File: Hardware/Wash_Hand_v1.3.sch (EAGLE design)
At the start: 32 parts, among them J1 I2C, J2 ICSP, J3 SPI, J5 EXT_VCC, J6 6_PIN_SERIAL_CABLEPTH, Q1 16.0 Mhz, U1 328P

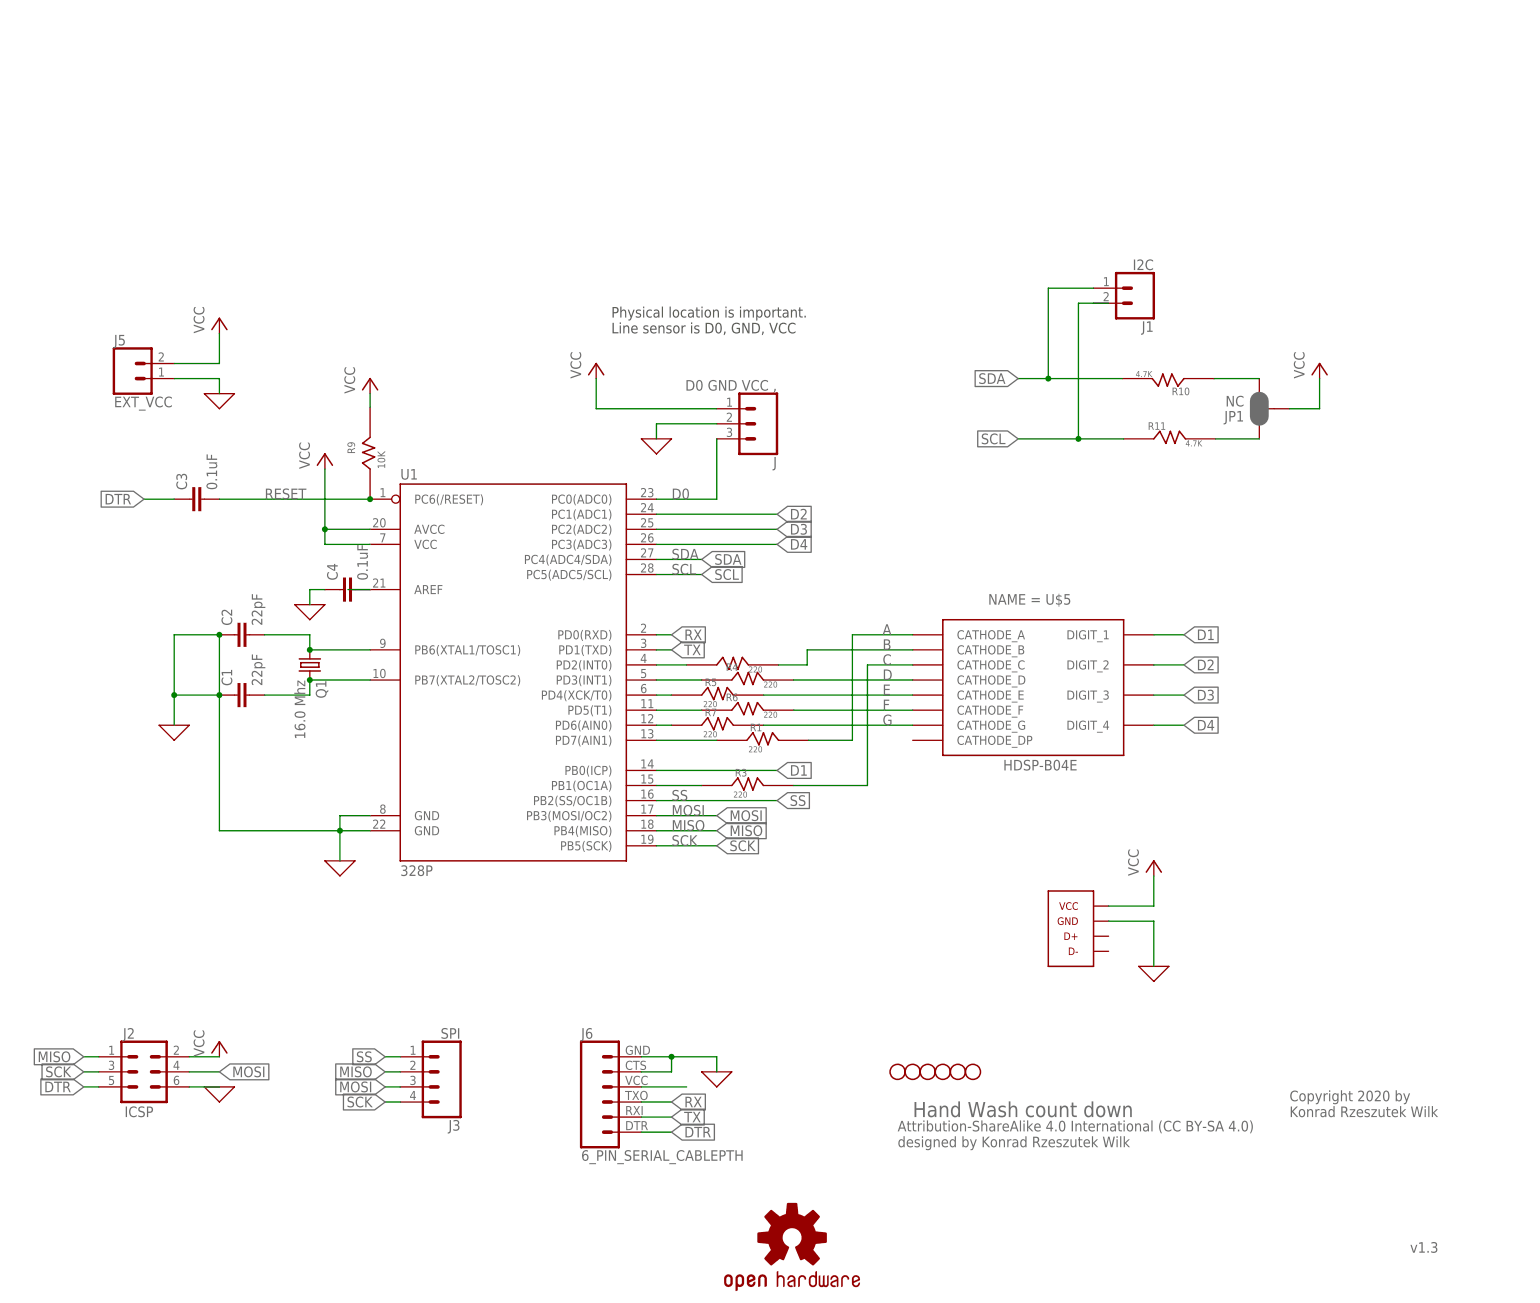
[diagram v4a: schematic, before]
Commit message: Board/Schematic: Add MIC5205 linear voltage regulator
Which also meant we had to:
 - Move resistors and capacitors around.
 - Move on the schematic the components around.
 - Instead of a switch I just added a solder pad to isolate the USB when not needed.

Signed-off-by: Konrad Rzeszutek Wilk <konrad@kernel.org>
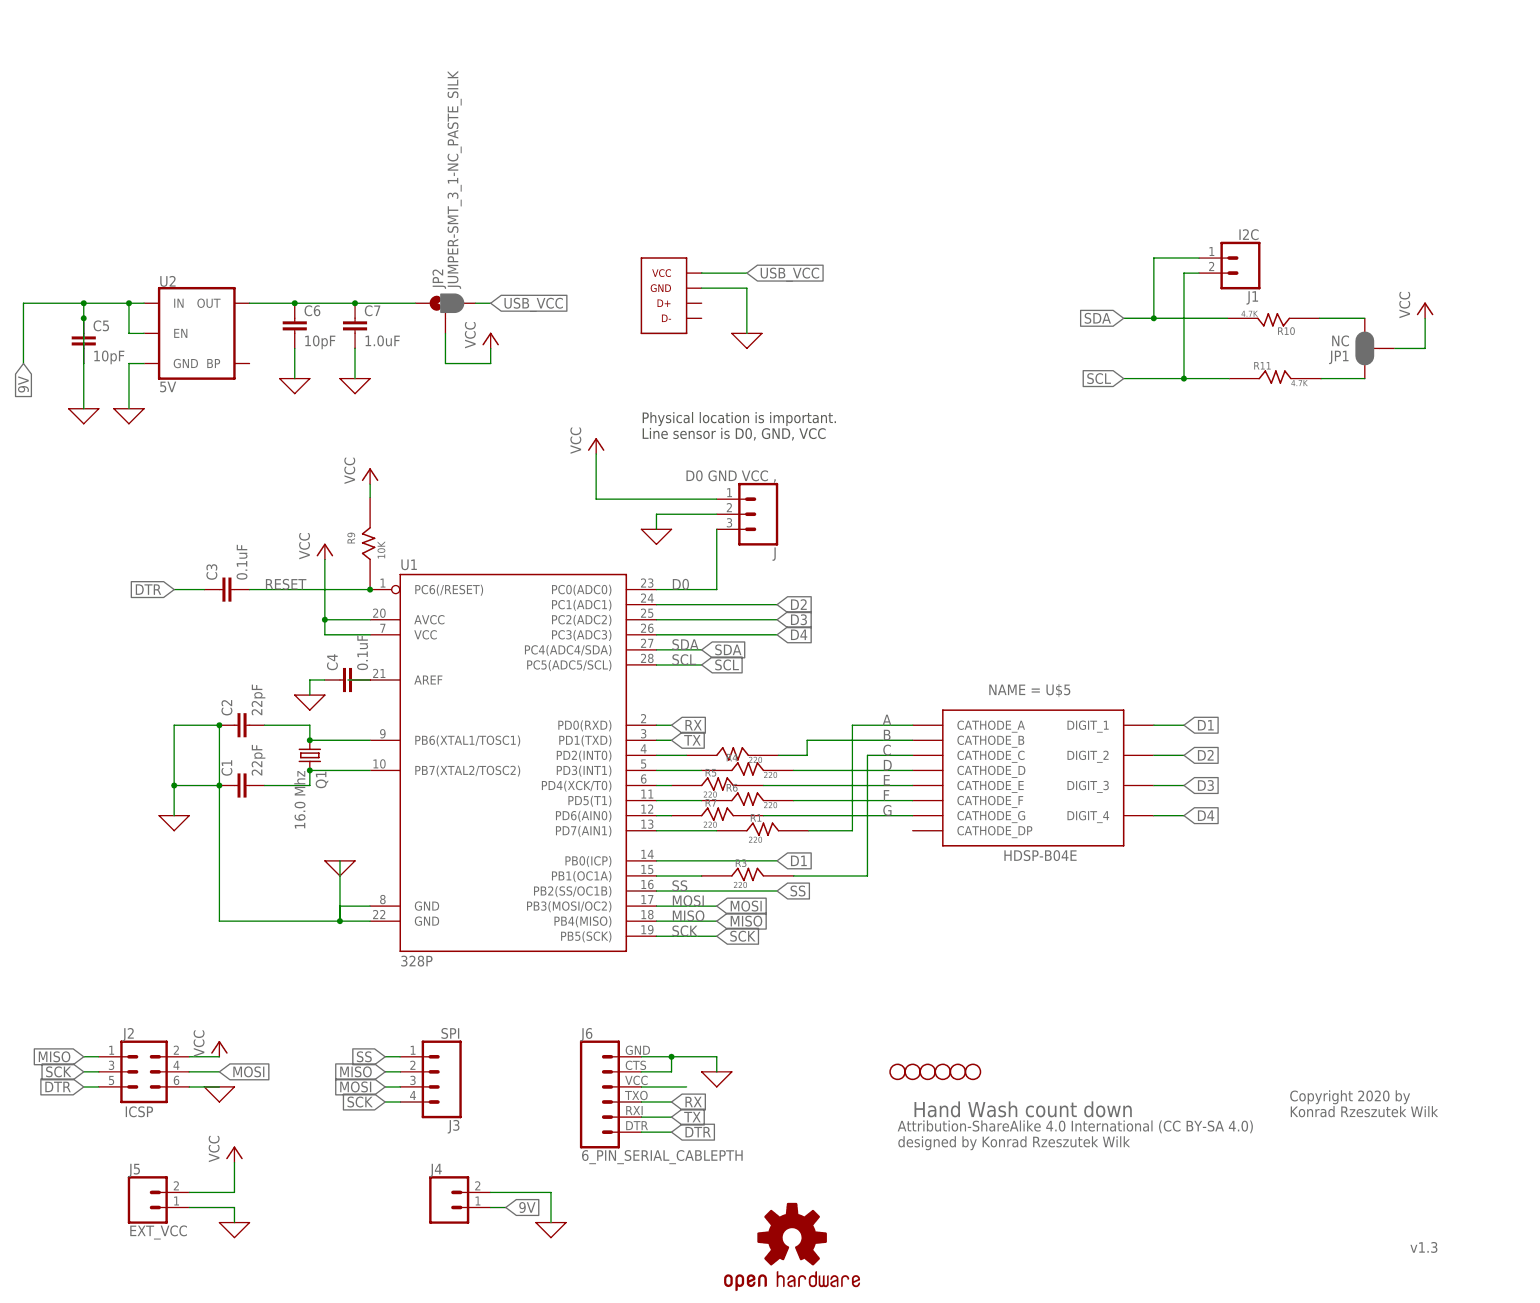
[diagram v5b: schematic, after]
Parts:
- added C5, C6: 10pF, SparkFun-Capacitors:1.0UF-1206-50V-10%
- added C7: 1.0uF, SparkFun-Capacitors:1.0UF-1206-50V-10%
- added J4: (no value), SparkFun-Connectors:CONN_02
- added JP2: JUMPER-SMT_3_1-NC_PASTE_SILK, SparkFun-Jumpers:JUMPER-SMT_3_1-NC_PASTE_SILK
- added U2: 5V, SparkFun-IC-Power:V_REG_MIC52055V
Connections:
- new net 9V: C5.1, C5.2, J4.1, U2.EN, U2.IN
- new net N$10: C6.1, C7.1, JP2.1, U2.OUT
- new net USB_VCC: JP2.3, U$4.VCC
- net 0: now also C6.2, C7.2, J4.2, U2.GND
- net VCC: now also JP2.2; no longer U$4.VCC
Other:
- moved on the sheet: C1, C2, C3, C4, J, J1, J5, JP1, NAME = U$5, Q1, R1, R10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

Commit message: Board/Schematic: Add line sensor.
We are using QRE1113GR.

Signed-off-by: Konrad Rzeszutek Wilk <konrad@kernel.org>
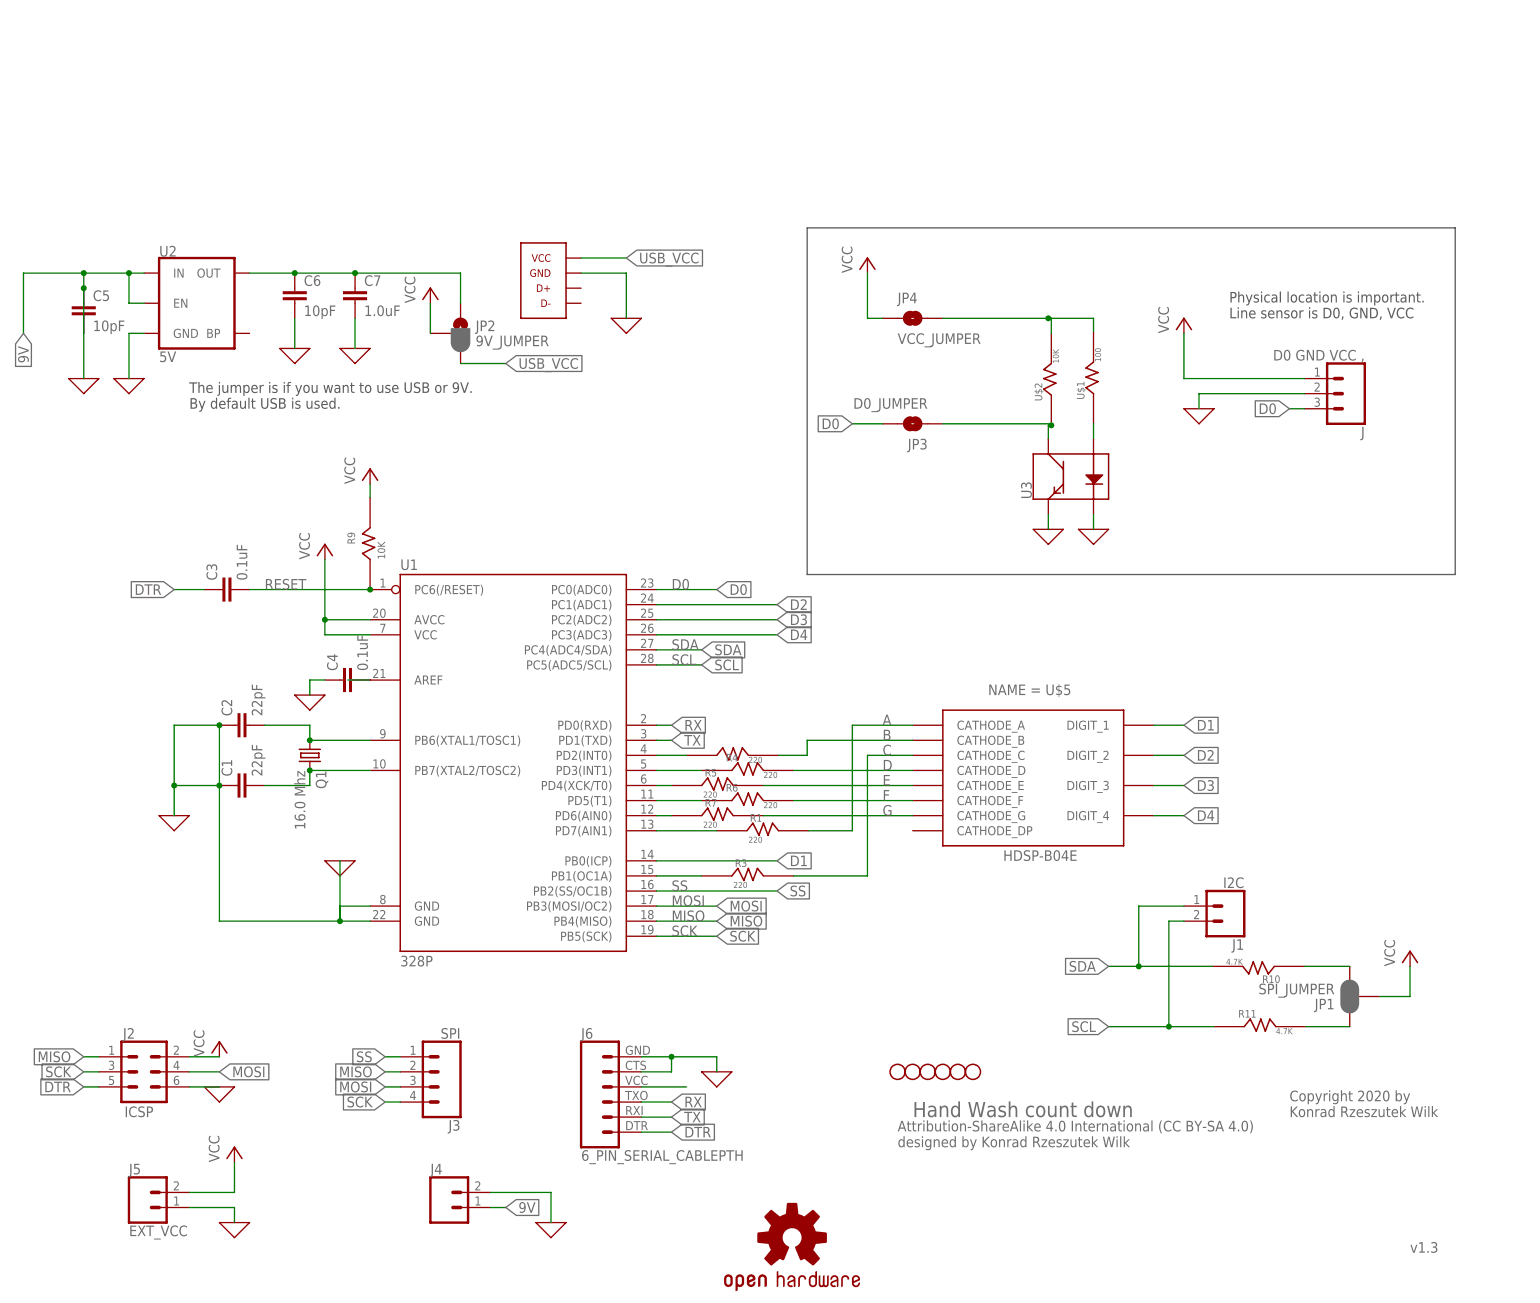
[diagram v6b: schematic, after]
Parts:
- added JP3: D0_JUMPER, SparkFun-Jumpers:JUMPER-SMT_2_NO_NO-SILK_ROUND
- added JP4: VCC_JUMPER, SparkFun-Jumpers:JUMPER-SMT_2_NO_NO-SILK_ROUND
- added U$1: 100, darnok_common:RESISTORR1206
- added U$2: 10K, darnok_common:RESISTORR1206
- added U3: (no value), SparkFun-Sensors:QRE1113SMD-W
- JP1: value NC -> SPI_JUMPER
- JP2: value JUMPER-SMT_3_1-NC_PASTE_SILK -> 9V_JUMPER
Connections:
- new net N$11: JP3.1, U$2.R_1, U3.C
- new net N$14: U$1.R_1, U3.A
- new net N$15: JP4.2, U$1.R_2, U$2.R_2
- net 0: now also U3.E, U3.K
- net D0: now also JP3.2
- net VCC: now also JP4.1
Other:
- note added: "The jumper is if you want to use USB or 9V. By default USB is used."
- moved on the sheet: C5, C6, C7, J, J1, JP1, JP2, R10, R11, U2

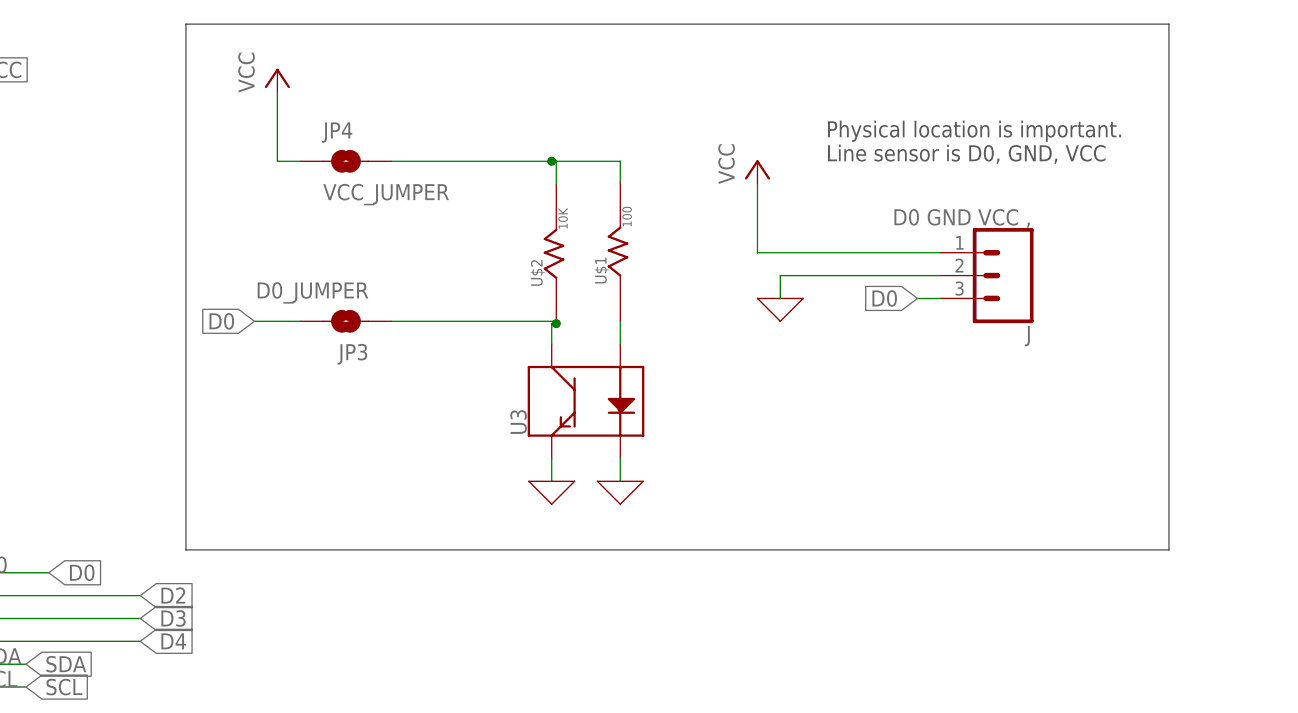
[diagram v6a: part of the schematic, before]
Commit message: Board: Change to different line sensor.
We are going to use discrete parts:
 - LTE-302, LTR-301 (IR emitter and detector).
 - TC33X-2-103E 10K pot
 - LM358DR
 - Bunch of SMD resistors

This should us give better range.

Signed-off-by: Konrad Rzeszutek Wilk <konrad@kernel.org>
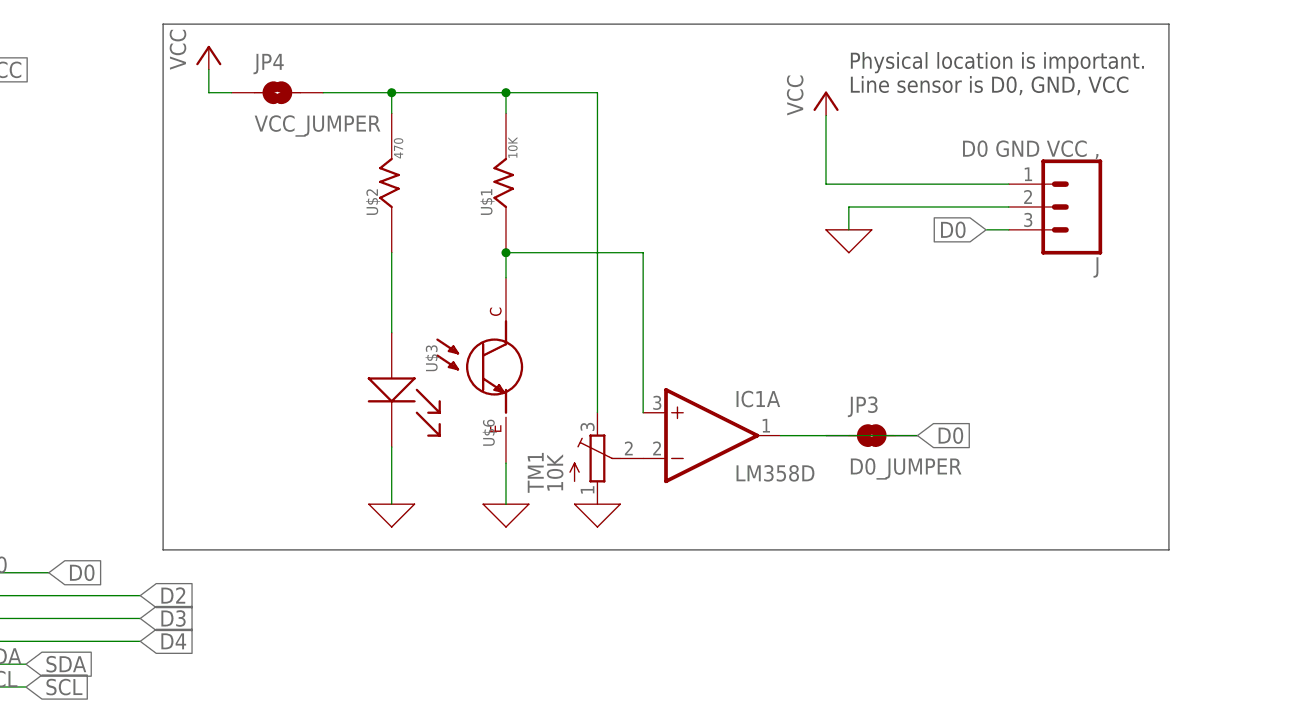
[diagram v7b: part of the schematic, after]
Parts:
- removed U3: (no value), SparkFun-Sensors:QRE1113SMD-W
- added IC1: LM358D, linear:LM358D
- added TM1: 10K, adafruit:TRIMPOTTC33X
- added U$3: LTE-302, darnok_sensors:LTE-302
- added U$6: LTR-301, darnok_sensors:LTR-301
- U$1: value 100 -> 10K
- U$2: value 10K -> 470
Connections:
- new net N$16: IC1A.-IN, TM1.S
- net 0: now also TM1.A, U$3.K$1, U$6.E$1; no longer U3.E, U3.K
- net D0: now also IC1A.OUT, JP3.1
- net N$11: now also U$3.A$1; no longer JP3.1, U3.C
- net N$14: now also IC1A.+IN, U$6.C$1; no longer U3.A
- net N$15: now also TM1.E
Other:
- moved on the sheet: J, JP3, JP4, U$1, U$2
